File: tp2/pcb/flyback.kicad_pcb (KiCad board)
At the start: 2 copper layers, 35 parts, among them J1 Conn_01x08_Socket, J2 Conn_01x08_Socket, Q1 2N2222, Q2 2N2907, Q3 TRBUZ80, Q4 BC547

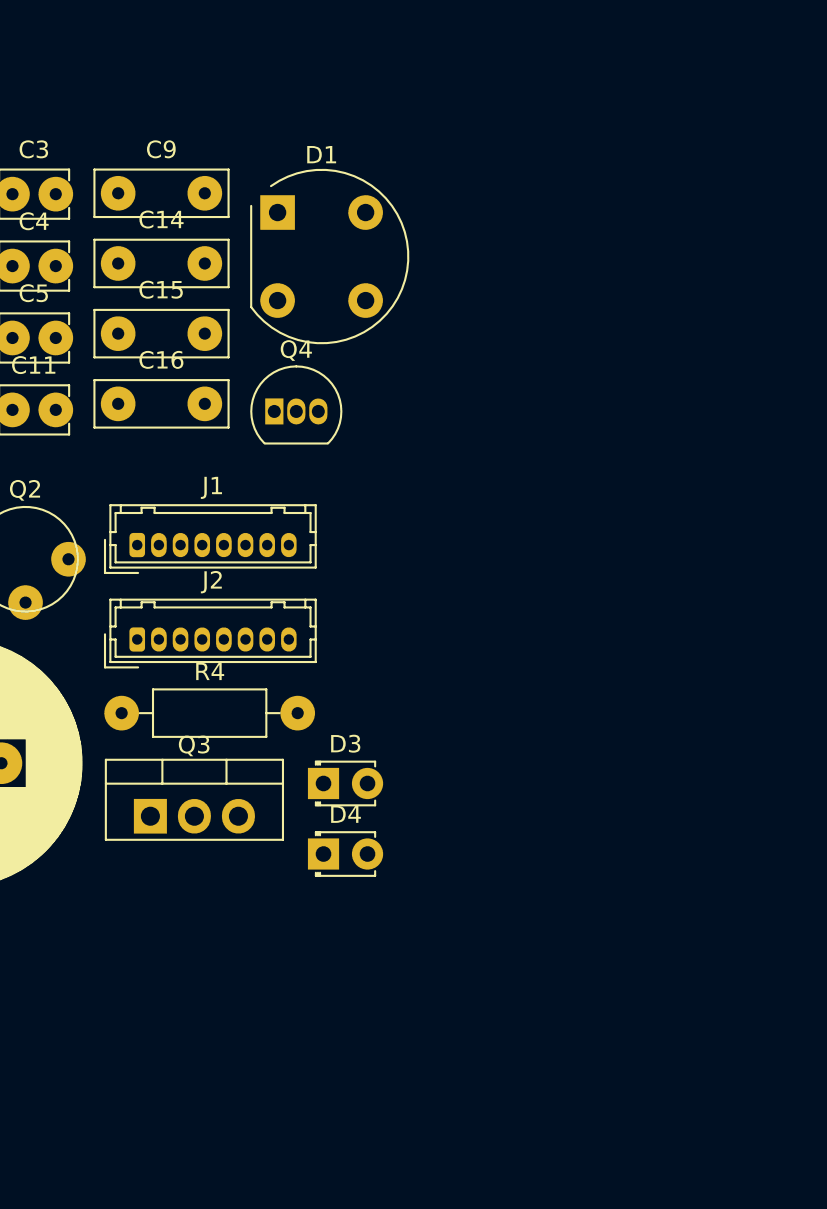
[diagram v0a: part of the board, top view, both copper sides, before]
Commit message: added almost all footprints to pcb
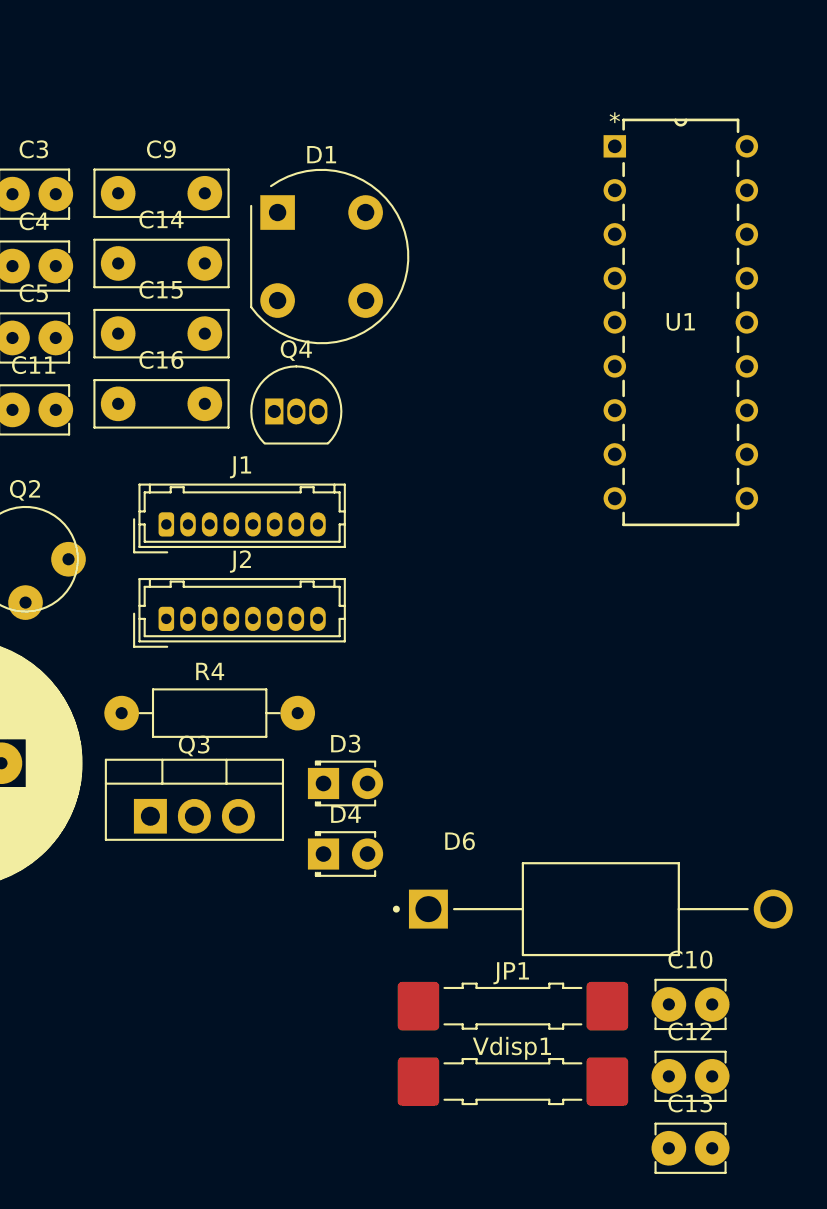
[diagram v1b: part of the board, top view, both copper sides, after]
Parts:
- added C10: 1n, TCLib:C_2.5mm, F.Cu at (127.5, 141.2)
- added C12: 47p, TCLib:C_2.5mm, F.Cu at (127.5, 145.3)
- added C13: 47p, TCLib:C_2.5mm, F.Cu at (127.5, 149.5)
- added D6: MUR460, MUR460(2):DIOAD1990W125L900D530, F.Cu at (123.6, 135.7)
- added JP1: Jumper_2_Bridged, Jumper:Jumper_Harwin_S1621_P10.9mm, F.Cu at (118.5, 141.3)
- added U1: UC3526AN, UC3536A:N18, F.Cu at (132.0, 112.0)
- added Vdisp1: Jumper_2_Bridged, Jumper:Jumper_Harwin_S1621_P10.9mm, F.Cu at (118.5, 145.7)
- J1, J2: value Conn_01x08_Socket -> 01x08_Pin
- moved J1 2.06 mm to (98.5, 113.5)
- moved J2 2.06 mm to (98.5, 119.0)
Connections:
- C6 pad 1: Net-(D1-+) -> Vin
- C9 pad 1: Net-(D1-+) -> Vin
- D2 pad A: Net-(J2-Pin_8) -> Net-(J1-Pin_1)
- D5 pad A: Net-(J2-Pin_1) -> Net-(J1-Pin_8)
- J1 pad 1: Vin -> Net-(J1-Pin_1)
- J1 pad 4: unconnected-(J1-Pin_4-Pad4) -> GNDREF
- J1 pad 5: unconnected-(J1-Pin_5-Pad5) -> GND
- J1 pad 8: Vdrain -> Net-(J1-Pin_8)
- J2 pad 1: Net-(J2-Pin_1) -> Vdrain
- J2 pad 4: GND -> unconnected-(J2-Pin_4-Pad4)
- J2 pad 5: GNDREF -> unconnected-(J2-Pin_5-Pad5)
- J2 pad 8: Net-(J2-Pin_8) -> Vin

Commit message: rutea facu
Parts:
- removed Q4: BC547, Package_TO_SOT_THT:TO-92_Inline
- added C7: C-50V, TCLib:C_2.5mm, F.Cu at (235.8, 55.0)
- added C8: C-50V, TCLib:C_2.5mm, F.Cu at (219.9, 82.7)
- added J3: Connector_2, Connector_AMASS:AMASS_XT30U-F_1x02_P5.0mm_Vertical, F.Cu at (211.6, 62.3)
- added J4: Connector_2, Connector_AMASS:AMASS_XT30U-F_1x02_P5.0mm_Vertical, F.Cu at (211.7, 72.4)
- added J5: Connector_2, Connector_AMASS:AMASS_XT30U-F_1x02_P5.0mm_Vertical, F.Cu at (247.8, 101.5)
- added J6: Connector_2, Connector_AMASS:AMASS_XT30U-F_1x02_P5.0mm_Vertical, F.Cu at (247.7, 91.6)
- added J7: Terminal_2, TCLib:Bornera_2_P5mm, F.Cu at (157.0, 22.3)
- added J8: Terminal_2, TCLib:Bornera_2_P5mm, F.Cu at (21.1, 23.3)
- added R7: R, TCLib:R_0.125W, F.Cu at (222.6, 54.9)
- added R8: R, TCLib:R_0.125W, F.Cu at (232.1, 82.9)
- J1, J2: value 01x08_Pin -> Connector_2; footprint Connector_Hirose:Hirose_DF13-08P-1.25DSA_1x08_P1.25mm_Vertical -> Connector_AMASS:AMASS_XT30U-F_1x02_P5.0mm_Vertical
- R3: value 120k-0.125W-800V -> 58k-1W; footprint TCLib:R_0.125W -> TCLib:R_1W
- moved U1 221.9 mm to (-89.2, 128.7)
- moved C10 199.0 mm to (-70.8, 157.3)
- moved C12 199.0 mm to (-70.8, 161.4)
- moved C13 199.0 mm to (-70.8, 165.6)
- moved Vdisp1 199.0 mm to (-79.8, 161.7)
- moved R15 183.0 mm to (247.1, 85.8), turned to 90 degrees
- moved R1 180.7 mm to (246.7, 60.4), turned to -90 degrees
- moved D4 150.9 mm to (246.7, 74.1), turned to 90 degrees
- moved C2 150.6 mm to (232.5, 99.7), turned to -90 degrees
- moved C16 150.0 mm to (244.1, 84.5), turned to 90 degrees
- moved D2 149.3 mm to (232.4, 62.3), turned to 180 degrees
- moved C1 149.3 mm to (229.1, 71.8), turned to -90 degrees
- moved C4 143.7 mm to (-47.2, 142.3)
- moved C14 143.2 mm to (236.2, 70.6), turned to -90 degrees
- moved D5 143.2 mm to (225.8, 90.2)
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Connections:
- C4 pad 2: Net-(Q4-B) -> Net-(Q1-B)
- D2 pad A: Net-(J1-Pin_1) -> Net-(D2-PadA)
- D5 pad A: Net-(J1-Pin_8) -> Net-(D5-PadA)
- J1 pad 1: Net-(J1-Pin_1) -> Vin
- J1 pad 2: unconnected-(J1-Pin_2-Pad2) -> Vin
- J2 pad 2: unconnected-(J2-Pin_2-Pad2) -> Vdrain
- R6 pad 2: Net-(Q4-B) -> Net-(Q1-B)
- U1 pad 13: unconnected-(U1-OUTPUT_A-Pad13) -> Vcontrol
- U1 pad 14: 16V -> Vrealim
- U1 pad 16: Vcontrol -> unconnected-(U1-OUTPUT_B-Pad16)
- U1 pad 17: Vref -> Vrealim
- U1 pad 2: Vrealim -> unconnected-(U1--ERROR-Pad2)
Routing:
- net Net-(D2-PadA): track 0.00 -> 5.00 mm
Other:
- board outline added: 100 x 100 mm

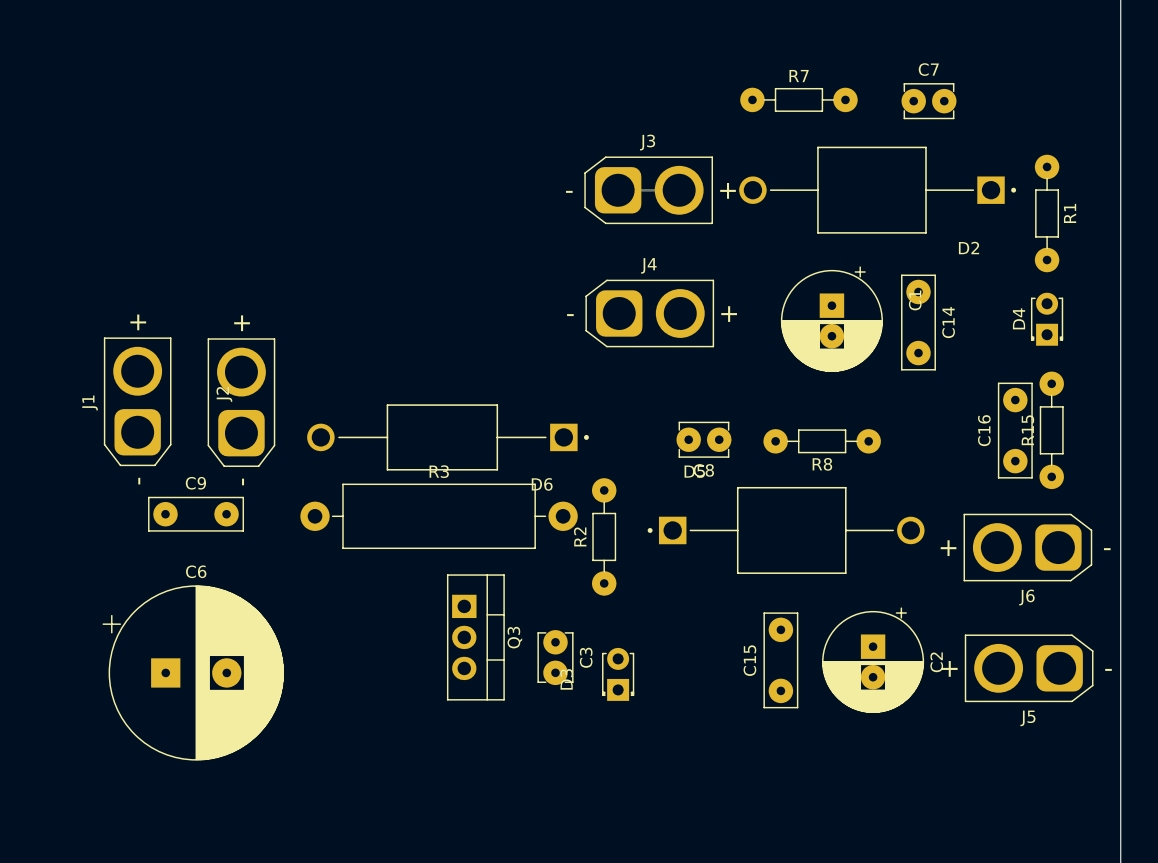
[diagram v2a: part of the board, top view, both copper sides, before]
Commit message: checkpoint antes de div res
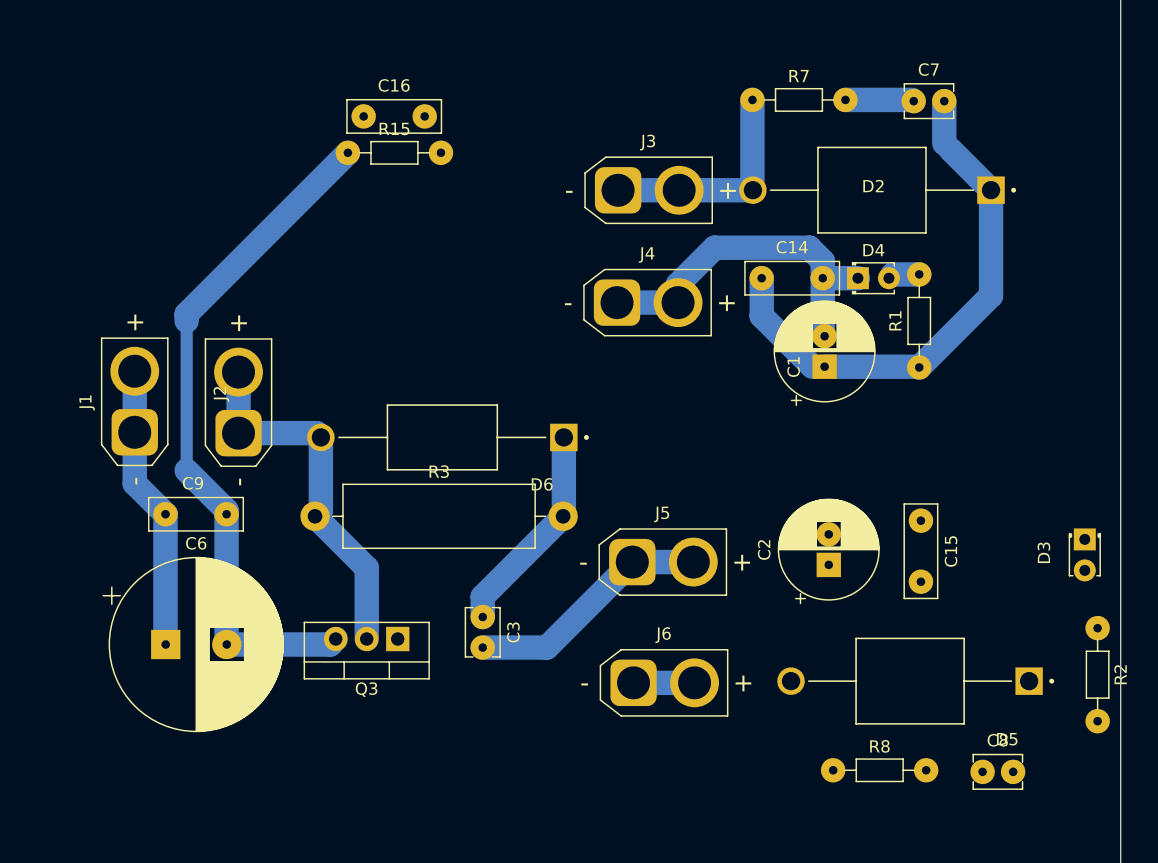
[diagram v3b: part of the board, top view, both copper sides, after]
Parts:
- moved R15 63.5 mm to (189.5, 59.2), turned to 0 degrees
- moved C16 60.4 mm to (190.8, 56.2), turned to 0 degrees
- moved R2 40.6 mm to (250.9, 98.2), turned to -90 degrees
- moved D3 40.2 mm to (249.8, 90.9), turned to -90 degrees
- moved J6 36.5 mm to (212.8, 102.6), turned to 0 degrees
- moved J5 36.1 mm to (212.8, 92.8), turned to 0 degrees
- moved C8 34.7 mm to (241.4, 109.9), turned to 0 degrees
- moved R8 27.1 mm to (229.2, 109.8), turned to 0 degrees
- moved R1 19.5 mm to (236.2, 76.8), turned to 90 degrees
- moved C15 18.1 mm to (236.4, 89.4), turned to -90 degrees
- moved D4 16.2 mm to (231.2, 69.5), turned to 0 degrees
- moved D5 15.7 mm to (235.5, 102.5), turned to 180 degrees
- moved C14 12.9 mm to (223.3, 69.5), turned to 0 degrees
- moved C2 7.62 mm to (228.8, 93.0), turned to 90 degrees
- moved C3 6.31 mm to (200.5, 97.2)
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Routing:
- net GND: track 0.00 -> 76.4 mm
- net Vout: track 0.00 -> 43.6 mm
- net Vdrain: track 0.00 -> 30.4 mm
- net GNDREF: track 0.00 -> 29.1 mm
- net Vin: track 0.00 -> 23.4 mm
- net Net-(C3-Pad1): track 0.00 -> 17.5 mm
- net Net-(D2-PadA): track 5.00 -> 19.1 mm
- net Net-(C7-Pad1): track 0.00 -> 5.63 mm
- net Net-(D5-PadA): track 0.00 -> 5.00 mm
- net Net-(D4-A): track 0.00 -> 2.61 mm

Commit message: ya rutie la flybuk
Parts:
- added R16: 10k, TCLib:R_0.25W, F.Cu at (214.2, 101.6)
- added R17: 3k9, TCLib:R_0.25W, F.Cu at (214.2, 98.4)
- added R20: 10k, TCLib:R_0.25W, F.Cu at (86.4, 109.8)
- added RV1: 10k, TCLib:RV_Preset_multivuelta_10mm_5mm, F.Cu at (87.8, 115.2)
- moved R1 19.4 mm to (237.9, 57.5), turned to -90 degrees
- moved J3 19.3 mm to (217.6, 43.9)
- moved R7 18.1 mm to (235.2, 42.0), turned to -90 degrees
- moved D3 17.7 mm to (232.3, 88.2), turned to 0 degrees
- moved R2 16.9 mm to (237.8, 87.5)
- moved C8 13.9 mm to (234.8, 97.7), turned to 90 degrees
- moved J4 13.1 mm to (217.5, 59.9)
- moved C15 12.0 mm to (224.3, 88.9), turned to 0 degrees
- moved D2 10.7 mm to (229.6, 51.9), turned to 90 degrees
- moved C16 10.0 mm to (198.8, 62.2)
- moved R15 10.0 mm to (197.5, 65.2)
- moved C2 10.0 mm to (226.8, 83.2), turned to 180 degrees
- moved R3 9.43 mm to (192.4, 81.4)
- moved C3 9.43 mm to (206.1, 89.7)
- moved C6 9.43 mm to (180.1, 91.9)
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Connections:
- U1 pad 1: Vref -> Vref'
- U1 pad 2: unconnected-(U1--ERROR-Pad2) -> Vrealim'
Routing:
- net Vrealim: track 0.00 -> 32.7 mm
- net Vout: track 43.6 -> 25.7 mm
- net Net-(D5-PadA): track 5.00 -> 18.1 mm
- net GND: track 76.4 -> 87.5 mm
- net Net-(C8-Pad1): track 0.00 -> 6.65 mm
- net GNDREF: track 29.1 -> 24.1 mm
- net Vrealim': track 0.00 -> 3.20 mm
- net Net-(D3-A): track 0.00 -> 3.17 mm
- net Net-(D2-PadA): track 19.1 -> 18.4 mm
- net Net-(D4-A): track 2.61 -> 3.17 mm

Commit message: por si me muero
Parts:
- removed JP1, Vdisp1: Jumper_2_Bridged, Jumper:Jumper_Harwin_S1621_P10.9mm
- added C17: 100n, TCLib:C_2.5mm, F.Cu at (194.2, 105.7)
- added J10: Connector_2, TCLib:PinHeader_1x02_P2.54mm_Vertical, F.Cu at (169.9, 92.1)
- added J9: Connector_2, TCLib:PinHeader_1x02_P2.54mm_Vertical, F.Cu at (203.4, 99.3)
- C12, C13: footprint TCLib:C_2.5mm -> TCLib:C_5mm
- D6: value MUR460 -> MUR160; footprint MUR460(2):DIOAD1990W125L900D530 -> MUR160:DIOAD1300W80L670D310
- moved U1 298.4 mm to (208.5, 108.4), turned to 90 degrees
- moved R9 276.1 mm to (204.9, 102.4), turned to 180 degrees
- moved R12 275.2 mm to (204.0, 122.3), turned to 180 degrees
- moved C10 272.2 mm to (198.7, 118.9), turned to 180 degrees
- moved R11 270.5 mm to (199.1, 124.7)
- moved R10 265.1 mm to (193.5, 126.1), turned to 90 degrees
- moved R5 260.5 mm to (189.3, 98.5)
- moved C11 256.7 mm to (205.9, 105.5)
- moved R13 256.2 mm to (184.9, 112.9), turned to -90 degrees
- moved R6 256.1 mm to (184.9, 104.7), turned to 180 degrees
- moved C13 251.9 mm to (177.6, 123.9), turned to 180 degrees
- moved R14 251.4 mm to (180.2, 121.1), turned to -90 degrees
- moved C12 248.3 mm to (174.1, 120.4), turned to 180 degrees
- moved C4 235.8 mm to (185.1, 101.6), turned to 180 degrees
- moved C5 211.9 mm to (160.9, 109.8)
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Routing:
- net GND: track 87.5 -> 318.3 mm
- net Vrealim: track 32.7 -> 95.8 mm
- net Vrealim': track 3.20 -> 44.0 mm
- net Vref: track 0.00 -> 32.8 mm
- net Net-(Q1-B): track 0.00 -> 29.2 mm
- net Net-(U1-COMP): track 0.00 -> 29.0 mm
- net Net-(Q1-E): track 0.00 -> 28.5 mm
- net Net-(C12-Pad1): track 0.00 -> 23.6 mm
- net 16V: track 0.00 -> 23.2 mm
- net Net-(C4-Pad1): track 0.00 -> 19.9 mm
- net Vref': track 0.00 -> 16.1 mm
- net Vneutro: track 0.00 -> 16.0 mm
- net Vcontrol: track 0.00 -> 10.2 mm
- net Net-(U1-RTIMING): track 0.00 -> 9.42 mm
- net Net-(U1-RESET*): track 0.00 -> 9.07 mm
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
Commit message: listo el routeo
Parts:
- added Rbridge1: 0, TCLib:R_0.125W, F.Cu at (211.8, 115.7)
- J1, J2, J3, J4, J5, J6: footprint Connector_AMASS:AMASS_XT30U-F_1x02_P5.0mm_Vertical -> TCLib:PinHeader_1x03_P2.54mm_Vertical
- moved Q3 17.8 mm to (203.2, 74.2)
- moved R3 13.6 mm to (191.4, 67.8)
- moved C6 13.2 mm to (170.3, 83.1)
- moved D6 12.3 mm to (197.5, 63.0)
- moved C16 9.58 mm to (159.7, 80.1)
- moved J10 9.55 mm to (163.8, 99.4)
- moved C9 9.37 mm to (177.5, 74.1)
- moved C3 8.85 mm to (214.9, 88.7), turned to 0 degrees
- moved R15 8.75 mm to (162.7, 80.1)
- moved R5 7.86 mm to (185.4, 105.3)
- moved J9 7.32 mm to (200.0, 105.8)
- moved J7 7.18 mm to (147.8, 109.5)
- moved R4 7.18 mm to (156.2, 117.4)
- moved C11 7.15 mm to (205.9, 112.7)
- moved C13 7.15 mm to (177.5, 131.1)
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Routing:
- net GNDREF: track 26.0 -> 100.5 mm
- net GND: track 318.3 -> 386.6 mm
- net Net-(Q3-G): track 7.96 -> 35.4 mm
- net Vref: track 32.8 -> 52.8 mm
- net Vin: track 31.2 -> 40.1 mm
- net Net-(C3-Pad1): track 24.4 -> 32.6 mm
- net Vrealim: track 95.8 -> 102.5 mm
- net Net-(Q1-E): track 28.5 -> 23.3 mm
- net Net-(D5-PadA): track 18.1 -> 23.1 mm
- net Vout: track 25.7 -> 30.1 mm
- net Net-(C4-Pad1): track 19.9 -> 16.9 mm
- net Net-(D2-PadA): track 18.4 -> 21.0 mm
- net Vlinea: track 8.70 -> 10.7 mm
- net Vneutro: track 16.0 -> 17.8 mm
- net Vdrain: track 30.5 -> 29.0 mm
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
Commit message: pcb quemado
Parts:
- added J11: Connector_3, TCLib:PinHeader_1x03_P2.54mm_Vertical, F.Cu at (164.9, 114.4)
- added REF**: ITBA_Bottom, TCLib:ITBA_Bottom, F.Cu at (230.3, 135.1)
- C5: footprint TCLib:C_2.5mm -> TCLib:C_5mm
- J1, J2, J3, J4, J5, J6: value Connector_2 -> Connector_3
- moved D4 21.0 mm to (238.0, 44.5), turned to -90 degrees
- moved J1 5.08 mm to (177.6, 64.0), turned to 0 degrees
- moved J2 5.00 mm to (186.2, 64.1), turned to 0 degrees
- moved J4 4.46 mm to (218.9, 59.8)
- moved J3 4.30 mm to (218.8, 44.1)
- moved R2 1.37 mm to (237.8, 93.3)
- moved J5 1.10 mm to (216.0, 93.7)
- moved R8 0.78 mm to (234.4, 116.8)
- moved C8 0.78 mm to (234.9, 102.8)
- moved D3 0.78 mm to (232.4, 93.2)
- moved D5 0.78 mm to (229.4, 106.8)
- moved C5 0.67 mm to (160.4, 117.4), turned to 90 degrees
- moved C15 0.61 mm to (224.5, 93.3)
- moved C2 0.52 mm to (226.9, 87.5)
- moved R1 0.47 mm to (238.3, 57.7), turned to 90 degrees
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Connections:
- C5 pad 1: 16V -> Vcol
- J1 pad 3: (no net) -> Vin
- J2 pad 3: (no net) -> Vdrain
- J3 pad 3: (no net) -> Net-(D2-PadA)
- J4 pad 3: (no net) -> GNDREF
- J5 pad 3: (no net) -> GND
- J6 pad 3: (no net) -> Net-(D5-PadA)
- Q1 pad 3: 16V -> Vcol
- R4 pad 1: 16V -> Vcol
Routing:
- net GNDREF: track 100.5 -> 123.2 mm
- net Vcol: track 0.00 -> 19.4 mm
- net Vrealim: track 102.5 -> 116.2 mm
- net GND: track 386.6 -> 397.0 mm
- net 16V: track 23.8 -> 17.1 mm
- net Vref: track 52.8 -> 49.4 mm
- net Net-(D2-PadA): track 21.0 -> 17.7 mm
- net Net-(D5-PadA): track 23.1 -> 24.4 mm
- net Net-(D3-A): track 2.26 -> 2.92 mm
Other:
- board text added: "Convertidor Volar-Atrás"

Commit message: agregue datasheets y linkee un modelo 3d
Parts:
- added REF**: Heatsink_AAVID_590302B03600G, Heatsink:Heatsink_AAVID_590302B03600G, F.Cu at (212.8, 87.9)
